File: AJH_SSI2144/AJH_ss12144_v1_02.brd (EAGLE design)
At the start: 19 x 106.8 mm, 57 parts, among them IC1 LM4040 5.0V, IC2 TL074D, IC3 TL072D, J100 PJ301_THONKICONN6, J101 PJ301_THONKICONN6, J102 PJ301_THONKICONN6, J103 PJ301_THONKICONN6, U1 BCM847BS

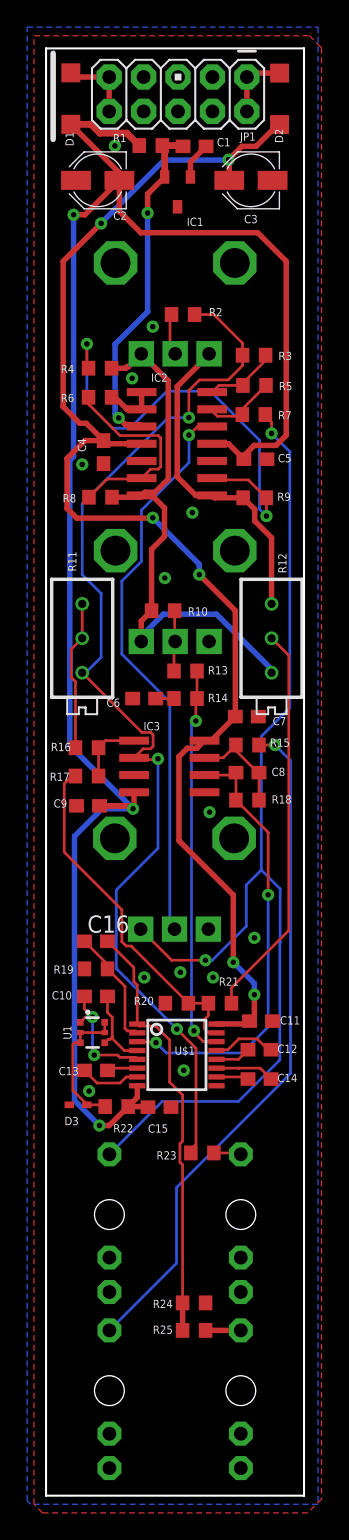
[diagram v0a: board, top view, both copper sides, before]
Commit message: Add 2B_VCA, add some comments on ssi2144 schematic
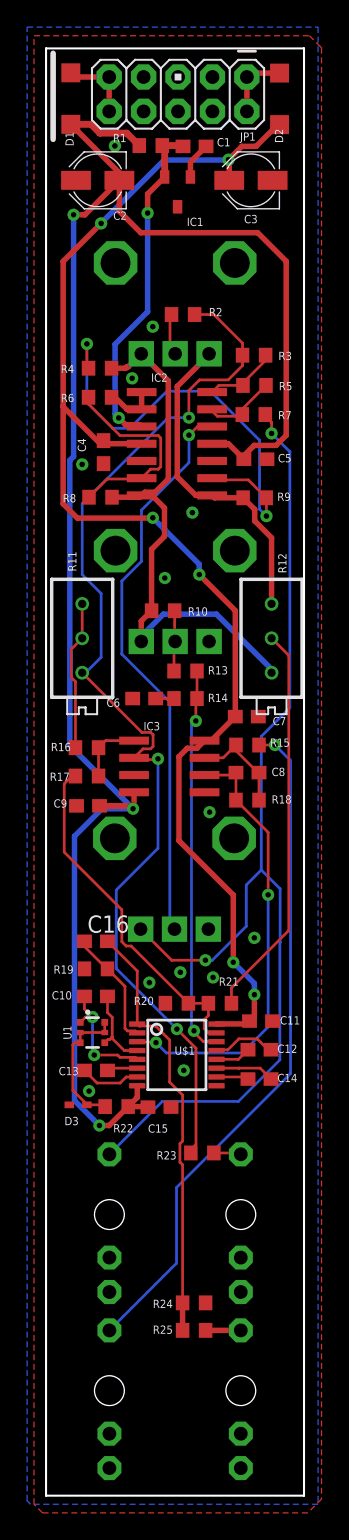
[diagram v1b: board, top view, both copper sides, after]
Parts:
- R16: value 162k -> 130k
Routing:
- net 12V: track 100.0 -> 100.9 mm
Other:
- board text added: "ssi2144 lpf v1.02, copyright forestcaver 2020"
- board text removed: "ssi2144 lpf v1.01, copyright forestcaver 2020"
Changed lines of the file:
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@@
 <wire x1="19.03" y1="106.76" x2="0" y2="106.76" width="0.1524" layer="20"/>
 <wire x1="0" y1="106.76" x2="0" y2="0" width="0.1524" layer="20"/>
-<text x="1.143" y="6.985" size="0.6096" layer="51" rot="R90">ssi2144 lpf v1.01, copyright forestcaver 2020</text>
+<text x="1.143" y="6.985" size="0.6096" layer="51" rot="R90">ssi2144 lpf v1.02, copyright forestcaver 2020</text>
 </plain>
 <attributes>
@@
 <attribute name="VALUE" x="9.218" y="85.098" size="1.27" layer="27"/>
 </element>
-<element name="R16" library="resistor" package="R0603" value="162k" x="3.022" y="55.175" smashed="yes">
+<element name="R16" library="resistor" package="R0603" value="130k" x="3.022" y="55.175" smashed="yes">
 <attribute name="NAME" x="0.355" y="54.921" size="0.6096" layer="25"/>
 <attribute name="VALUE" x="2.133" y="53.143" size="1.27" layer="27"/>
@@
 <via x="12.319" y="38.227" extent="1-16" drill="0.4064"/>
 <via x="9.906" y="38.608" extent="1-16" drill="0.4064"/>
-<via x="7.239" y="38.227" extent="1-16" drill="0.4064"/>
+<via x="7.62" y="37.846" extent="1-16" drill="0.4064"/>
 <via x="15.367" y="41.148" extent="1-16" drill="0.4064"/>
 <via x="12.065" y="50.419" extent="1-16" drill="0.4"/>
@@
 <wire x1="8.71305" y1="98.5238" x2="4.064" y2="93.87475" width="0.4064" layer="16"/>
 <wire x1="4.064" y1="93.853" x2="4.064" y2="93.87475" width="0.4064" layer="16"/>
-<wire x1="1.2634" y1="80.32770625" x2="2.48770625" y2="79.1034" width="0.4064" layer="1"/>
-<wire x1="2.48770625" y1="79.1034" x2="2.9696" y2="79.1034" width="0.4064" layer="1"/>
-<wire x1="2.9696" y1="79.1034" x2="4.242" y2="77.831" width="0.4064" layer="1"/>
 <wire x1="4.064" y1="93.853" x2="1.2634" y2="91.0524" width="0.4064" layer="1"/>
 <wire x1="1.2634" y1="91.0524" x2="1.2634" y2="80.32770625" width="0.4064" layer="1"/>
 <via x="7.874" y="72.136" extent="1-16" drill="0.4064"/>
-<wire x1="1.5484" y1="72.82770625" x2="2.26470625" y2="72.1114" width="0.4064" layer="1"/>
+<wire x1="2.3106" y1="72.1114" x2="1.2634" y2="73.1586" width="0.4064" layer="1"/>
 <wire x1="7.874" y1="72.136" x2="7.8494" y2="72.1114" width="0.4064" layer="1"/>
-<wire x1="7.8494" y1="72.1114" x2="2.26470625" y2="72.1114" width="0.4064" layer="1"/>
-<wire x1="4.242" y1="77.831" x2="2.86510625" y2="77.831" width="0.4064" layer="1"/>
-<wire x1="2.86510625" y1="77.831" x2="1.5484" y2="76.51429375" width="0.4064" layer="1"/>
-<wire x1="1.5484" y1="76.51429375" x2="1.5484" y2="72.82770625" width="0.4064" layer="1"/>
+<wire x1="7.8494" y1="72.1114" x2="2.3106" y2="72.1114" width="0.4064" layer="1"/>
 <wire x1="11.303" y1="68.707" x2="11.303" y2="67.945" width="0.4064" layer="16"/>
 <wire x1="11.303" y1="68.707" x2="7.874" y2="72.136" width="0.4064" layer="16"/>
@@
 <wire x1="14.798" y1="34.798" x2="12.588" y2="34.798" width="0.4064" layer="1"/>
 <wire x1="14.798" y1="34.798" x2="15.01" y2="35.01" width="0.4064" layer="1"/>
+<wire x1="1.2634" y1="80.32770625" x2="3.99410625" y2="77.597" width="0.4064" layer="1"/>
+<wire x1="3.99410625" y1="77.597" x2="4.476" y2="77.597" width="0.4064" layer="1"/>
+<wire x1="1.2634" y1="73.1586" x2="1.2634" y2="80.32770625" width="0.4064" layer="1"/>
 </signal>
 <signal name="10V" class="1">
@@
 <wire x1="8.255" y1="47.752" x2="8.255" y2="54.356" width="0.2032" layer="16"/>
 <wire x1="8.255" y1="54.356" x2="8.199" y2="54.3" width="0.2032" layer="1"/>
-<wire x1="14.495" y1="84.127" x2="14.495" y2="85.016" width="0.2032" layer="1"/>
 <wire x1="14.495" y1="85.016" x2="12.381" y2="87.13" width="0.2032" layer="1"/>
 <wire x1="12.381" y1="87.13" x2="10.957" y2="87.13" width="0.2032" layer="1"/>
-<wire x1="14.48465" y1="84.127" x2="14.495" y2="84.127" width="0.2032" layer="1"/>
 <via x="10.5378" y="79.52178125" extent="1-16" drill="0.4"/>
-<wire x1="14.495" y1="84.127" x2="14.495" y2="83.365" width="0.2032" layer="1"/>
 <wire x1="14.495" y1="83.365" x2="13.4354" y2="82.3054" width="0.2032" layer="1"/>
 <wire x1="13.4354" y1="82.3054" x2="11.31935" y2="82.3054" width="0.2032" layer="1"/>
@@
 <wire x1="2.667" y1="67.945" x2="4.064" y2="66.548" width="0.2032" layer="16"/>
 <wire x1="2.667" y1="60.706" x2="7.0712" y2="56.3018" width="0.2032" layer="1"/>
+<wire x1="14.495" y1="84.127" x2="14.495" y2="85.016" width="0.2032" layer="1"/>
+<wire x1="14.495" y1="84.127" x2="14.495" y2="83.365" width="0.2032" layer="1"/>
 </signal>
 <signal name="N$10">
@@
 <wire x1="5.8222" y1="37.5728" x2="5.8222" y2="34.46075" width="0.2032" layer="1"/>
 <contactref element="C16" pad="1"/>
-<wire x1="2.833" y1="40.894" x2="4.533" y2="39.194" width="0.2032" layer="1"/>
-<wire x1="4.533" y1="39.194" x2="4.533" y2="38.862" width="0.2032" layer="1"/>
+<wire x1="2.833" y1="40.894" x2="2.833" y2="40.513" width="0.2032" layer="1"/>
+<wire x1="4.533" y1="38.862" x2="4.484" y2="38.862" width="0.2032" layer="1"/>
+<wire x1="4.484" y1="38.862" x2="2.833" y2="40.513" width="0.2032" layer="1"/>
 </signal>
 <signal name="N$25">
@@
 <wire x1="10.0718" y1="29.5522" x2="9.1142" y2="30.5098" width="0.2032" layer="1"/>
 <contactref element="C16" pad="2"/>
-<wire x1="6.477" y1="37.91136875" x2="6.727" y2="37.66136875" width="0.2032" layer="1"/>
-<wire x1="6.727" y1="37.66136875" x2="6.727" y2="34.787" width="0.2032" layer="1"/>
-<wire x1="4.533" y1="40.894" x2="6.477" y2="38.95" width="0.2032" layer="1"/>
-<wire x1="6.477" y1="38.95" x2="6.477" y2="37.91136875" width="0.2032" layer="1"/>
+<wire x1="4.533" y1="40.894" x2="6.727" y2="38.7" width="0.2032" layer="1"/>
+<wire x1="6.727" y1="38.7" x2="6.727" y2="34.787" width="0.2032" layer="1"/>
 </signal>
 <signal name="LOWPASS_OUT">
